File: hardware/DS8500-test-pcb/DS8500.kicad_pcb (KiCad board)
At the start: 2 copper layers, 25 parts, among them P1 POWER, P2 INTERFACE, U1 AP1117V5, U2 DS8500, Y1 3.6864MHz

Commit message: PCB - WIP
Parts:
- JP1, JP2, JP3: value Jumper_NO_Small -> (none)
- moved P1 51.8 mm to (110.7, 93.1), turned to 180 degrees
- moved W3 47.5 mm to (121.0, 102.6)
- moved W4 45.0 mm to (201.2, 97.4)
- moved U1 41.0 mm to (119.1, 92.2), turned to 180 degrees
- moved P2 39.3 mm to (110.7, 97.5)
- moved U2 37.0 mm to (132.2, 98.9), turned to 315 degrees
- moved R4 35.1 mm to (116.6, 97.9)
- moved R3 31.1 mm to (116.6, 100.1), turned to 180 degrees
- moved R2 26.9 mm to (116.6, 104.8)
- moved R1 26.9 mm to (116.6, 102.6), turned to 180 degrees
- moved C4 26.5 mm to (175.3, 78.7)
- moved C3 25.0 mm to (175.2, 76.7)
- moved W1 24.5 mm to (197.1, 97.4)
- moved W2 23.6 mm to (196.0, 102.4)
- moved C1 23.5 mm to (114.4, 91.9), turned to 90 degrees
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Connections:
- U2 pad 21: (no net) -> GND
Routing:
- net GND: track 0.00 -> 25.1 mm
- net VCC: track 0.00 -> 7.38 mm
- net +5V: track 0.00 -> 6.64 mm
- net Net-(P2-Pad3): track 0.00 -> 4.89 mm
- net Net-(P2-Pad2): track 0.00 -> 4.89 mm
- net Net-(JP1-Pad2): track 0.00 -> 2.16 mm
- net Net-(R3-Pad2): track 0.00 -> 2.16 mm

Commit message: Beta(?) version of the PCB
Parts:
- removed JP1, JP2: , Pin_Headers:Pin_Header_Straight_1x02
- removed R2: 20k, w_smd_resistors:r_0805
- P2: footprint Pin_Headers:Pin_Header_Straight_1x03 -> Pin_Headers:Pin_Header_Straight_1x02
- R1: value 10k -> 0
- moved W2 79.3 mm to (116.7, 104.6)
- moved C3 52.4 mm to (130.4, 103.9)
- moved C6 50.9 mm to (126.4, 91.4), turned to 270 degrees
- moved W4 50.6 mm to (150.6, 99.6)
- moved C4 48.0 mm to (134.4, 103.9), turned to 180 degrees
- moved C7 46.9 mm to (130.3, 89.8)
- moved W1 46.6 mm to (150.6, 94.1)
- moved C5 41.4 mm to (136.0, 91.9), turned to 90 degrees
- moved Y1 36.4 mm to (132.3, 100.2), turned to 180 degrees
- moved C9 31.7 mm to (142.0, 91.1)
- moved C8 30.4 mm to (142.0, 97.2)
- moved R1 15.2 mm to (128.8, 93.5), turned to 270 degrees
- moved JP3 14.3 mm to (140.7, 94.1), turned to 90 degrees
- moved U2 4.95 mm to (132.3, 94.0), turned to 270 degrees
- moved W3 2.79 mm to (122.2, 100.1)
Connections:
- R1 pad 1: Net-(P2-Pad3) -> Net-(R1-Pad1)
- R1 pad 2: Net-(JP1-Pad2) -> Net-(R1-Pad2)
- R3 pad 2: Net-(R3-Pad2) -> Net-(R1-Pad1)
- R4 pad 1: Net-(R3-Pad2) -> Net-(R1-Pad1)
- U2 pad 20: Net-(R3-Pad2) -> Net-(R1-Pad2)
- U2 pad 6: Net-(JP1-Pad2) -> GND
- W3 pad 1: Net-(JP1-Pad2) -> Net-(R1-Pad1)
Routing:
- net VCC: track 7.38 -> 35.1 mm, vias 0 -> 2
- net Net-(R1-Pad1): track 0.00 -> 17.6 mm
- net Net-(C8-Pad1): track 0.00 -> 13.7 mm
- net Net-(C8-Pad2): track 0.00 -> 12.9 mm
- net Net-(C4-Pad2): track 0.00 -> 9.85 mm
- net Net-(C3-Pad2): track 0.00 -> 9.29 mm
- net Net-(P2-Pad3): track 4.89 -> 0.00 mm
- net GND: track 25.1 -> 28.5 mm
- net Net-(R1-Pad2): track 0.00 -> 2.76 mm
- net Net-(C5-Pad2): track 0.00 -> 2.65 mm
- net Net-(JP1-Pad2): track 2.16 -> 0.00 mm
- net Net-(R3-Pad2): track 2.16 -> 0.00 mm
- added copper zone on F.Cu, net GND
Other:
- board outline added: 45.7 x 21.6 mm

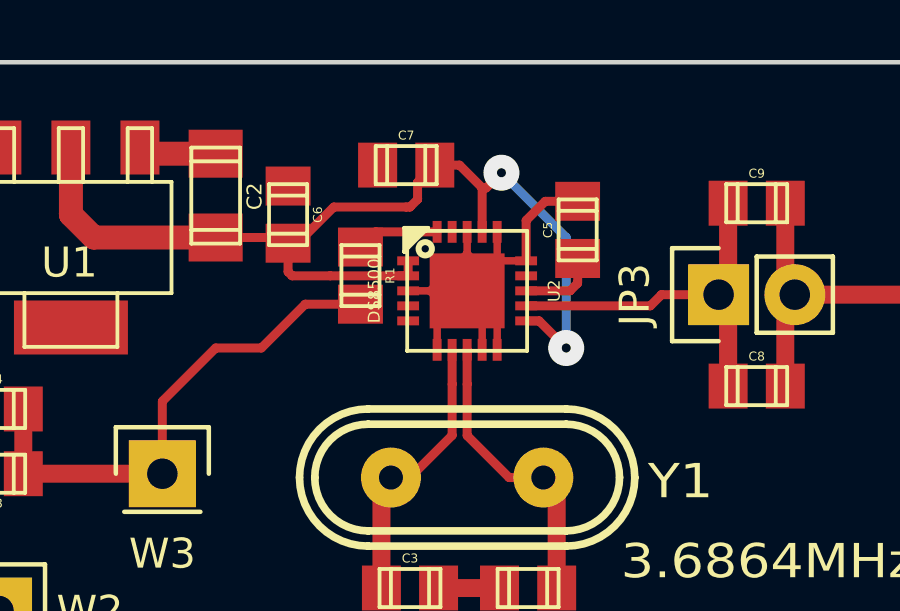
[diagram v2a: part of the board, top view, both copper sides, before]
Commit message: Some minor changes to the flood fill
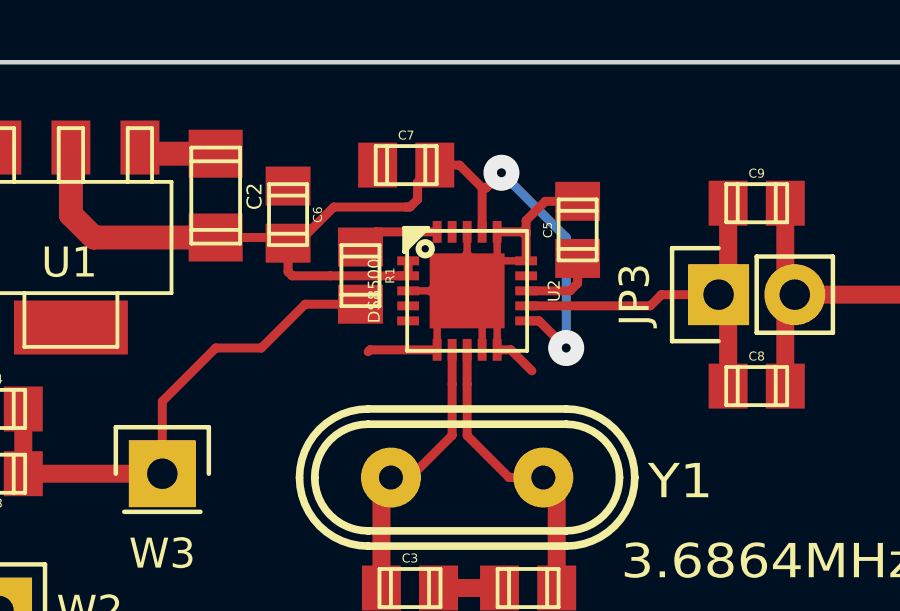
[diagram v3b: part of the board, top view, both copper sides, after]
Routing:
- net GND: track 28.5 -> 33.4 mm
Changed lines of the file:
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@@
   (general
     (links 48)
-    (no_connects 0)
-    (area 107.874999 86.284999 153.745001 108.025001)
+    (no_connects 1)
+    (area 106.952 79.7 167.004 108.025001)
     (thickness 1.6)
-    (drawings 4)
-    (tracks 105)
+    (drawings 6)
+    (tracks 113)
     (zones 0)
     (modules 22)
@@
     (visible_elements FFFFFF7F)
     (pcbplotparams
-      (layerselection 0x00030_80000001)
+      (layerselection 0x00000_00000001)
       (usegerberextensions false)
-      (excludeedgelayer true)
+      (excludeedgelayer false)
       (linewidth 0.100000)
       (plotframeref false)
@@
       (psnegative false)
       (psa4output false)
-      (plotreference true)
-      (plotvalue true)
+      (plotreference false)
+      (plotvalue false)
       (plotinvisibletext false)
       (padsonsilk false)
       (subtractmaskfromsilk false)
-      (outputformat 1)
+      (outputformat 2)
       (mirror false)
       (drillshape 1)
@@
     )
   )
+  (dimension 21.59 (width 0.3) (layer Cmts.User)
+    (gr_text "21,590 mm" (at 160.354 97.155 270) (layer Cmts.User)
+      (effects (font (size 1.5 1.5) (thickness 0.3)))
+    )
+    (feature1 (pts (xy 153.67 107.95) (xy 161.704 107.95)))
+    (feature2 (pts (xy 153.67 86.36) (xy 161.704 86.36)))
+    (crossbar (pts (xy 159.004 86.36) (xy 159.004 107.95)))
+    (arrow1a (pts (xy 159.004 107.95) (xy 158.417579 106.823496)))
+    (arrow1b (pts (xy 159.004 107.95) (xy 159.590421 106.823496)))
+    (arrow2a (pts (xy 159.004 86.36) (xy 158.417579 87.486504)))
+    (arrow2b (pts (xy 159.004 86.36) (xy 159.590421 87.486504)))
+  )
+  (dimension 45.72 (width 0.3) (layer Cmts.User)
+    (gr_text "45,720 mm" (at 130.81 81.2) (layer Cmts.User)
+      (effects (font (size 1.5 1.5) (thickness 0.3)))
+    )
+    (feature1 (pts (xy 153.67 86.36) (xy 153.67 79.85)))
+    (feature2 (pts (xy 107.95 86.36) (xy 107.95 79.85)))
+    (crossbar (pts (xy 107.95 82.55) (xy 153.67 82.55)))
+    (arrow1a (pts (xy 153.67 82.55) (xy 152.543496 83.136421)))
+    (arrow1b (pts (xy 153.67 82.55) (xy 152.543496 81.963579)))
+    (arrow2a (pts (xy 107.95 82.55) (xy 109.076504 83.136421)))
+    (arrow2b (pts (xy 107.95 82.55) (xy 109.076504 81.963579)))
+  )
   (gr_line (start 153.67 86.36) (end 107.95 86.36) (angle 90) (layer Edge.Cuts) (width 0.15))
   (gr_line (start 153.67 107.95) (end 153.67 86.36) (angle 90) (layer Edge.Cuts) (width 0.15))
@@
   (segment (start 115.52174 89.20226) (end 116.82476 89.20226) (width 0.8) (layer F.Cu) (net 1))
   (segment (start 114.173 90.551) (end 115.52174 89.20226) (width 0.8) (layer F.Cu) (net 1))
-  (segment (start 134.29996 92.97924) (end 134.29996 91.63304) (width 0.3) (layer F.Cu) (net 2))
+  (segment (start 133.33476 92.01404) (end 134.29996 92.01404) (width 0.3) (layer F.Cu) (net 2))
+  (segment (start 134.239 92.075) (end 134.29996 92.075) (width 0.3) (layer F.Cu) (net 2))
+  (segment (start 134.29996 92.01404) (end 134.239 92.075) (width 0.3) (layer F.Cu) (net 2))
+  (segment (start 133.33476 95.94596) (end 133.79196 95.94596) (width 0.3) (layer F.Cu) (net 2))
+  (segment (start 133.79196 95.94596) (end 134.493 96.647) (width 0.3) (layer F.Cu) (net 2))
+  (segment (start 131.33324 95.94596) (end 129.09804 95.94596) (width 0.3) (layer F.Cu) (net 2))
+  (segment (start 129.09804 95.94596) (end 129.032 96.012) (width 0.3) (layer F.Cu) (net 2))
+  (segment (start 134.29996 92.97924) (end 134.29996 92.075) (width 0.3) (layer F.Cu) (net 2))
+  (segment (start 134.29996 92.075) (end 134.29996 91.63304) (width 0.3) (layer F.Cu) (net 2))
+  (segment (start 134.29996 91.63304) (end 134.9375 90.9955) (width 0.3) (layer F.Cu) (net 2))
   (segment (start 134.9375 90.9955) (end 136.017 90.9955) (width 0.3) (layer F.Cu) (net 2))
-  (segment (start 134.29996 91.63304) (end 134.9375 90.9955) (width 0.3) (layer F.Cu) (net 2))
   (segment (start 130.36804 93.98) (end 131.08432 93.98) (width 0.25) (layer F.Cu) (net 2))
   (segment (start 131.08432 93.98) (end 131.70916 94.60484) (width 0.25) (layer F.Cu) (net 2))
@@
   (zone (net 2) (net_name GND) (layer F.Cu) (hatch edge 0.508)
     (connect_pads (clearance 0.5))
-    (min_thickness 0.25)
+    (min_thickness 0.5)
     (fill yes (arc_segments 16) (thermal_gap 0.508) (thermal_bridge_width 0.508))
     (polygon

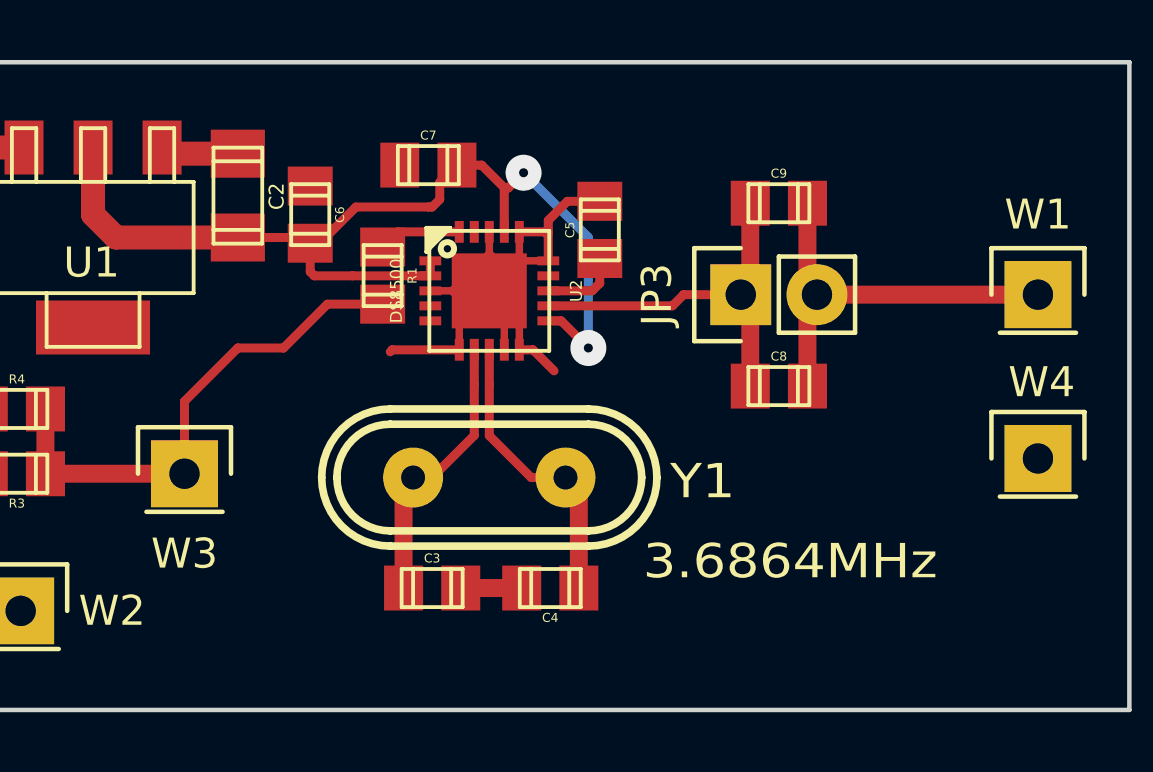
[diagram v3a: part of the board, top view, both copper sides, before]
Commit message: Wrong package for DS8500. The correct one is TQFN-20 5x5mm
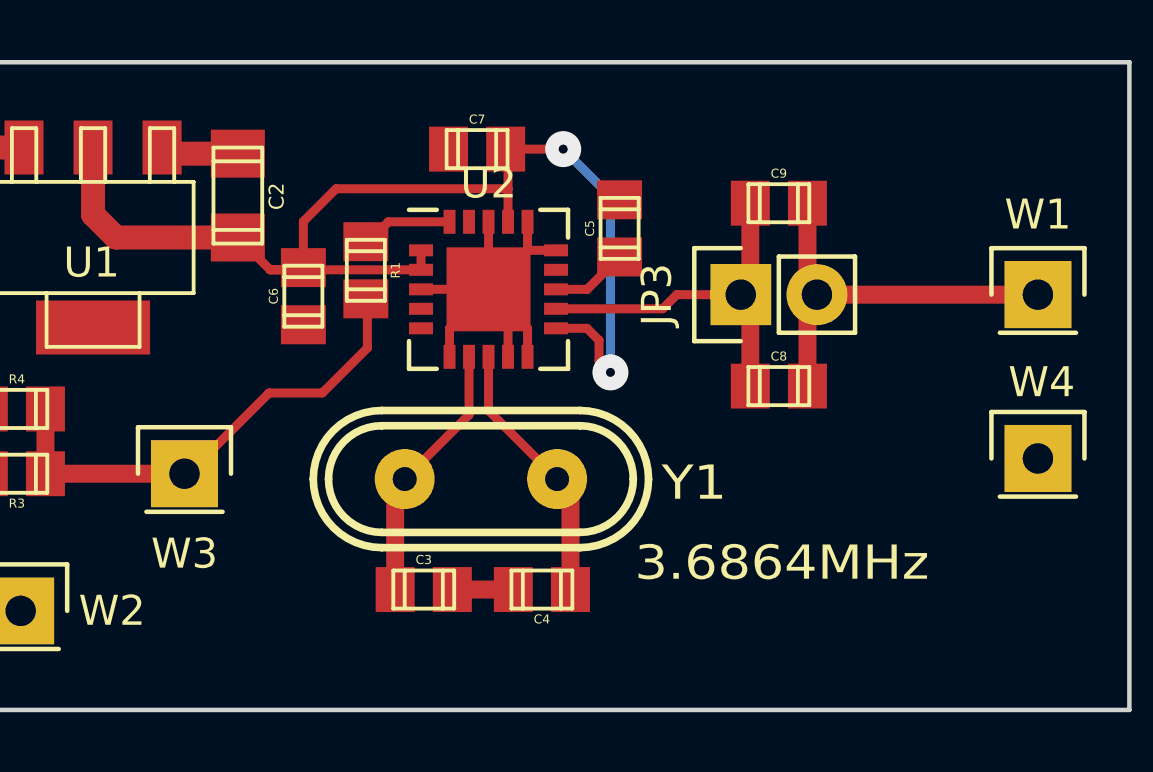
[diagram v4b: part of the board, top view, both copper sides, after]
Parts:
- U2: footprint w_smd_qfn:qfn-20 -> Housings_DFN_QFN:QFN-20-1EP_5x5mm_Pitch0.65mm
- moved C6 2.73 mm to (126.1, 94.2), turned to 90 degrees
- moved C7 1.71 mm to (131.9, 89.3)
- moved C5 0.66 mm to (136.7, 91.9)
- moved R1 0.59 mm to (128.2, 93.3)
- moved C3 0.28 mm to (130.1, 103.9)
- moved C4 0.28 mm to (134.1, 103.9)
- moved Y1 0.28 mm to (132.1, 100.3)
- moved U2 0.06 mm to (132.3, 93.9), turned to 0 degrees
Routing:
- net VCC: track 35.1 -> 40.2 mm
- net GND: track 33.4 -> 36.1 mm
- net Net-(C4-Pad2): track 9.85 -> 8.89 mm
- net Net-(R1-Pad1): track 17.6 -> 16.8 mm

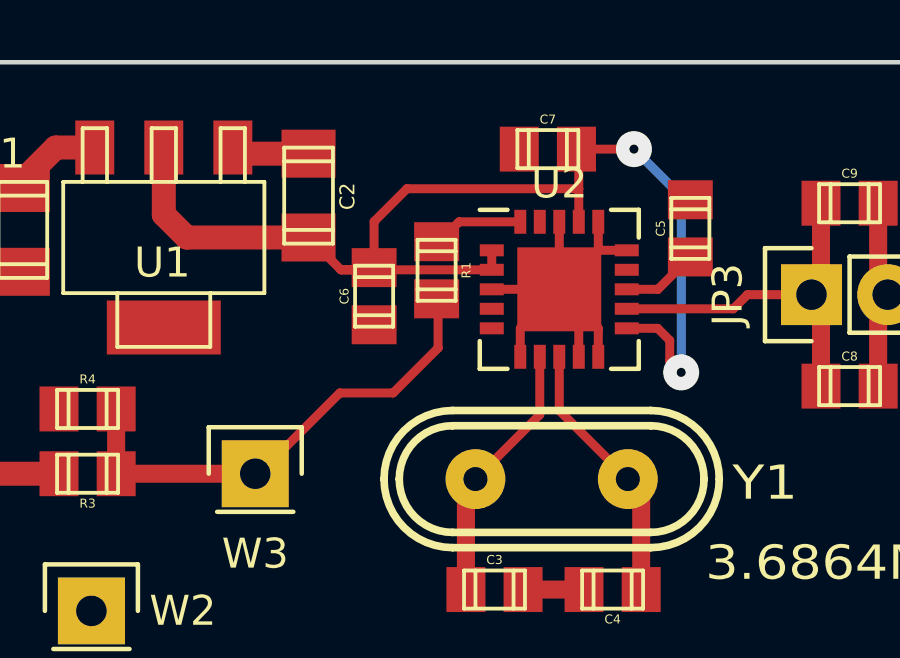
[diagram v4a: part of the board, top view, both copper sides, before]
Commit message: Extended the leads of the TQFN-20 for hand soldering
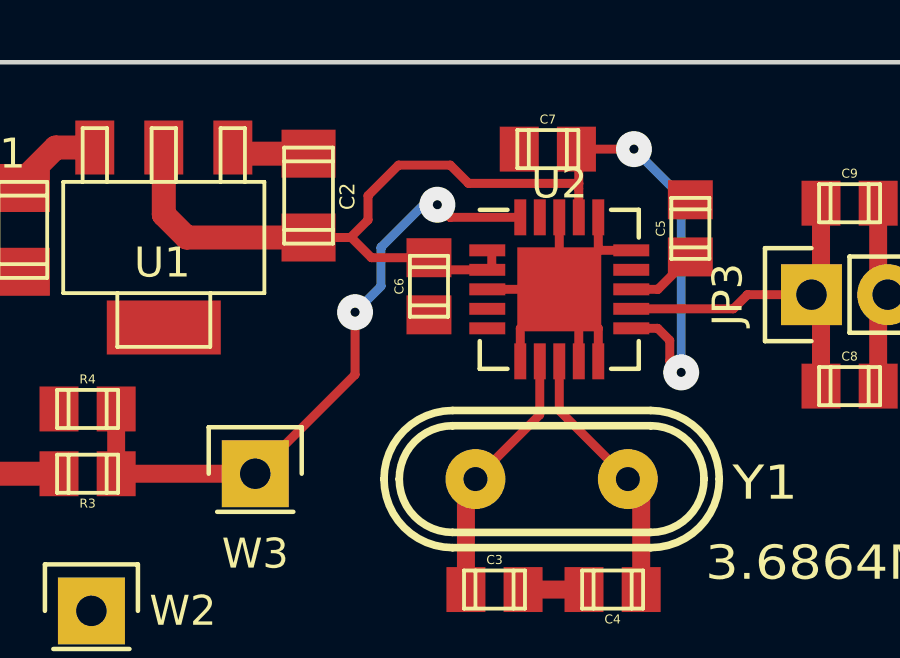
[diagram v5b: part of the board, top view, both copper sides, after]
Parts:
- removed R1: 0, w_smd_resistors:r_0805
- moved C6 1.86 mm to (128.0, 93.8)
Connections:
- R3 pad 2: Net-(R1-Pad1) -> Net-(R3-Pad2)
- R4 pad 1: Net-(R1-Pad1) -> Net-(R3-Pad2)
- U2 pad 20: Net-(R1-Pad2) -> Net-(R3-Pad2)
- U2 pad 21: GND -> (no net)
- W3 pad 1: Net-(R1-Pad1) -> Net-(R3-Pad2)
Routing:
- net Net-(R3-Pad2): track 0.00 -> 22.1 mm, vias 0 -> 2
- net Net-(R1-Pad1): track 16.8 -> 0.00 mm
- net GND: track 36.1 -> 31.0 mm
- net (no net): track 0.00 -> 5.02 mm
- net Net-(R1-Pad2): track 3.06 -> 0.00 mm
- net VCC: track 40.2 -> 39.2 mm

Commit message: One more extension of the leads
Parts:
- moved C6 0.33 mm to (127.6, 93.8)
- moved C7 0.20 mm to (131.9, 89.1)
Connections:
- U2 pad 21: (no net) -> GND
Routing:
- net GND: track 31.0 -> 36.1 mm
- net (no net): track 5.02 -> 0.00 mm
- net VCC: track 39.2 -> 38.6 mm
